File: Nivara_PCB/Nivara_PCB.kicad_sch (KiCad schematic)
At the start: 16 parts, among them J1 NPN_IN, J10 ANALOG_OUT, J11 RELAY, J2 PNP_IN, J3 D_IN, J4 ANALOG_IN, J5 RUN/STOP, J6 FUENTE, J7 NPN_OUT, J8 PNP_OUT, J9 RS485, U4 2920L185DR

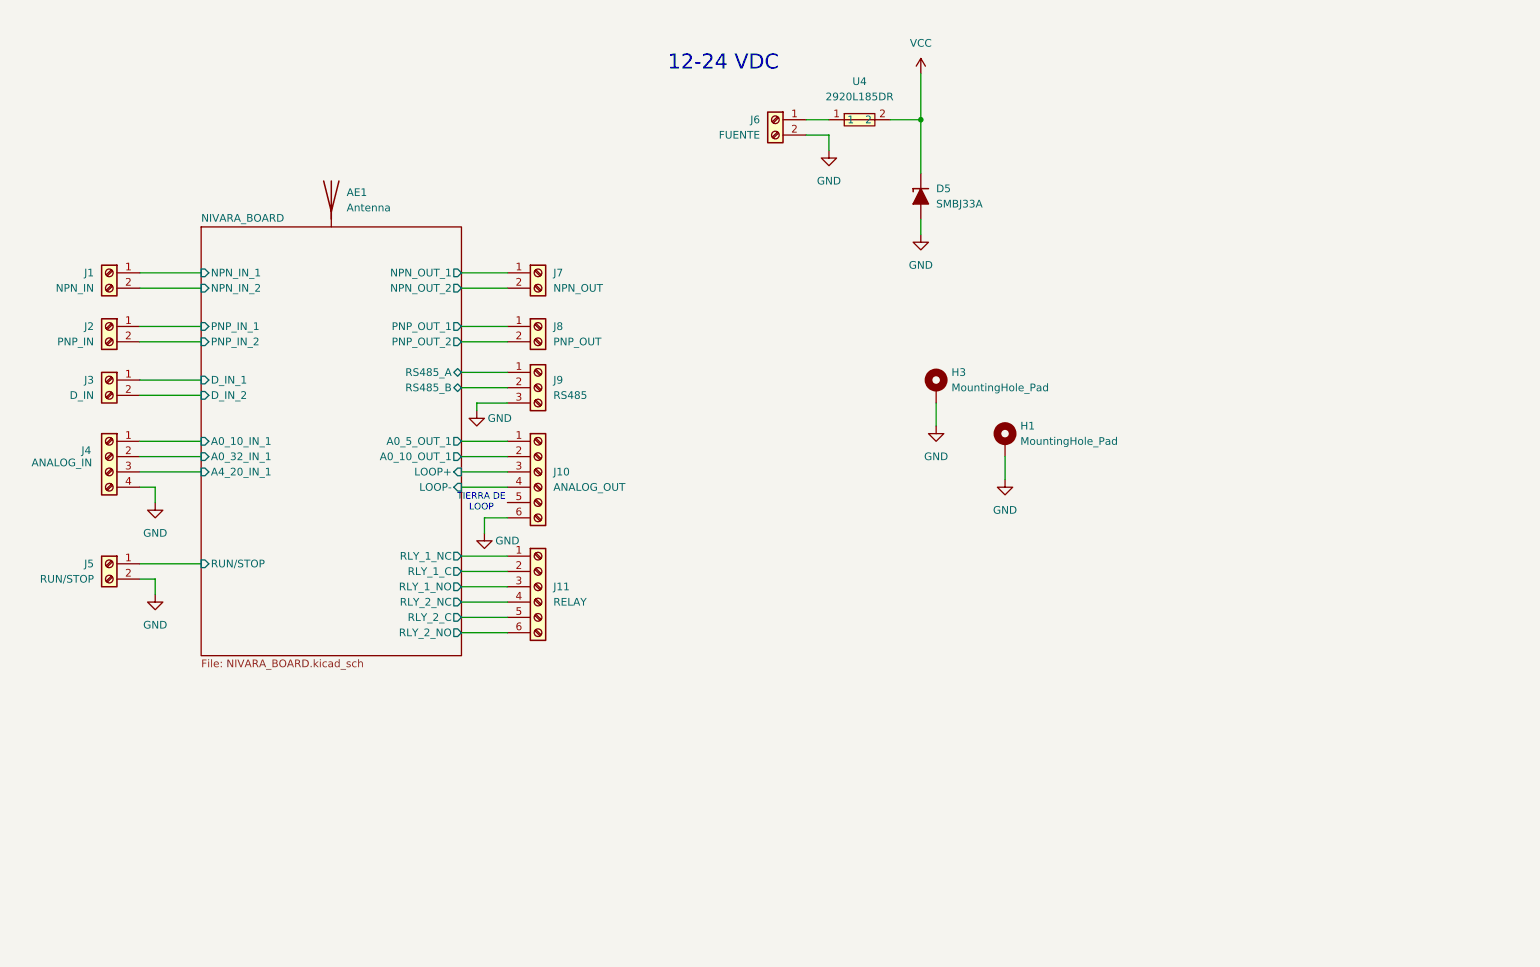
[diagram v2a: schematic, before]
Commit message: Cambios en la medición de voltaje y corriente de la PCB Nivara.
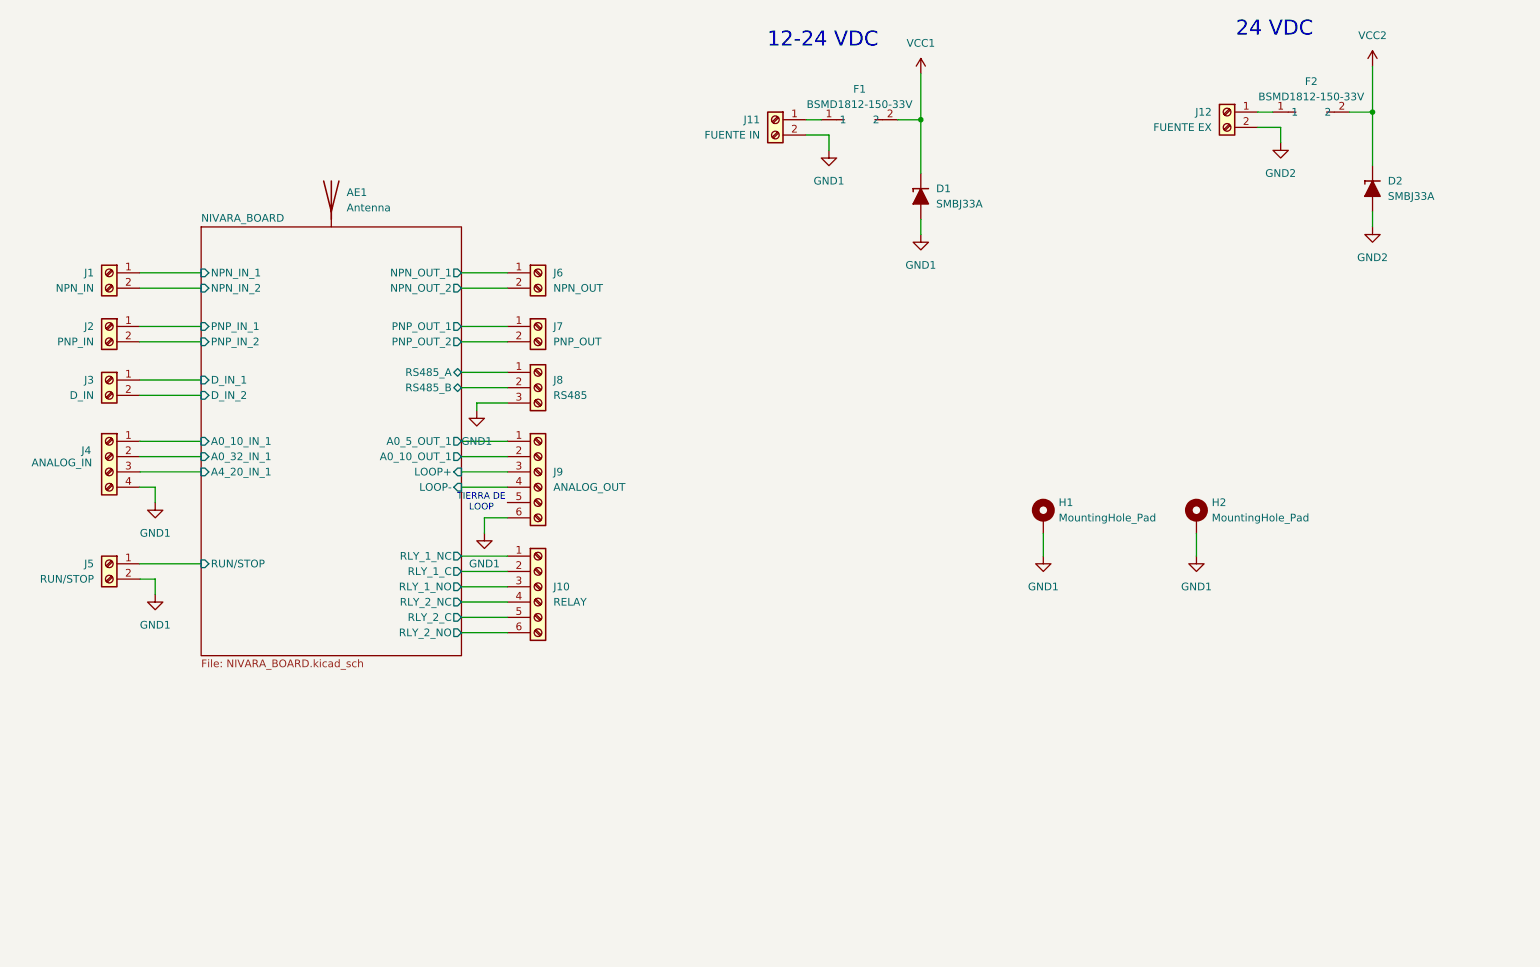
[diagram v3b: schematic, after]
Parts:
- removed U4: 2920L185DR, Fuse_Holder:F2920, symbol Fuse_Holder:2920L185DR
- added D2: SMBJ33A, PCM_Diode_SMD_AKL:D_SMB, symbol PCM_Diode_TVS_AKL:SMBJ33A
- added F1, F2: BSMD1812-150-33V, EasyEDA:F1812, symbol EasyEDA:BSMD1812-150-33V
- added J12: FUENTE EX, TerminalBlock:TerminalBlock_bornier-2_P5.08mm, symbol Connector:Screw_Terminal_01x02
- J11: renamed from J6; value FUENTE -> FUENTE IN
- renumbered D5 to D1, H3 to H1, H1 to H2, J11 to J10, J7 to J6, J8 to J7, J9 to J8, J10 to J9
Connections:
- net at J11.1 (Pin_1): now also F1.1
- net GND renamed GND1
- net VCC renamed VCC1
- net VCC1: now also F1.2
- new net: F2.1, J12.1 (Pin_1)
- new net GND2: D2.2 (A), J12.2 (Pin_2)
- new net VCC2: D2.1 (K), F2.2
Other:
- note added: "24 VDC"
- moved on the sheet: H1, H2

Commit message: New changes to the Nivara PCB schematic files.
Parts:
- removed J9: ANALOG_OUT, TerminalBlock:TerminalBlock_bornier-6_P5.08mm, symbol Connector:Screw_Terminal_01x06
- added C19: 100nF, PCM_Capacitor_SMD_AKL:C_0603_1608Metric, symbol PCM_Capacitor_US_AKL:C_0603
- added D23: SM712, PCM_Package_TO_SOT_SMD_AKL:SOT-23, symbol PCM_Diode_TVS_AKL:SM712
- added J13: USB_C_Receptacle_USB2.0_14P, symbol Connector:USB_C_Receptacle_USB2.0_14P
- added J14: PINHD_1x2_Female, Connector_PinSocket_2.54mm:PinSocket_1x02_P2.54mm_Vertical, symbol PCM_SL_Pin_Headers:PINHD_1x2_Female
- added J9: ANALOG_OUT., TerminalBlock:TerminalBlock_bornier-3_P5.08mm, symbol Connector:Screw_Terminal_01x03
- added R50, R51: 5.1k, PCM_Resistor_SMD_AKL:R_0805_2012Metric, symbol PCM_Resistor_US_AKL:R_0805
- added R52: 10k, PCM_Resistor_SMD_AKL:R_0603_1608Metric, symbol PCM_Resistor_US_AKL:R_0603
- added R53: 14k, PCM_Resistor_SMD_AKL:R_0603_1608Metric, symbol PCM_Resistor_US_AKL:R_0603
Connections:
- net GND1: now also C19.2, D23.3 (Com), J13.A1 (GND), J13.A12 (GND), J13.B1 (GND), J13.B12 (GND), J9.3 (Pin_3), R50.2, R51.2, R53.1
- net NIVARA_BOARD/A0_10_IN_1: now also J4.2 (Pin_2); no longer J4.1 (Pin_1)
- net NIVARA_BOARD/A0_32_IN_1: now also J4.3 (Pin_3); no longer J4.2 (Pin_2)
- net NIVARA_BOARD/A4_20_IN_1: now also J4.1 (Pin_1); no longer J4.3 (Pin_3)
- new net: J13.A4 (VBUS), J13.A9 (VBUS), J13.B4 (VBUS), J13.B9 (VBUS), R52.2
- new net: J13.A5 (CC1), R51.1
- new net: J13.B5 (CC2), R50.1
- new net: C19.1, J13.S1 (SHIELD)
- new net NIVARA_BOARD/A0_V_OUT_1: J9.1 (Pin_1)
- new net NIVARA_BOARD/AUX_1: J14.1
- new net NIVARA_BOARD/AUX_2: J14.2
- new net NIVARA_BOARD/I_OUT: J9.2 (Pin_2)
- new net NIVARA_BOARD/USB_D+: D23.2 (A2), J13.A6 (D+), J13.B6 (D+)
- new net NIVARA_BOARD/USB_D-: D23.1 (A1), J13.A7 (D-), J13.B7 (D-)
- new net NIVARA_BOARD/Vbus: R52.1, R53.2
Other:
- sheet NIVARA_BOARD ports: added A0_V_OUT_1, AUX_1, AUX_2, I_OUT, USB_D+, USB_D-, Vbus; removed A0_10_OUT_1, A0_5_OUT_1, LOOP+, LOOP-
- note removed: "TIERRA DE LOOP"
- moved on the sheet: AE1, H1, H2, J10

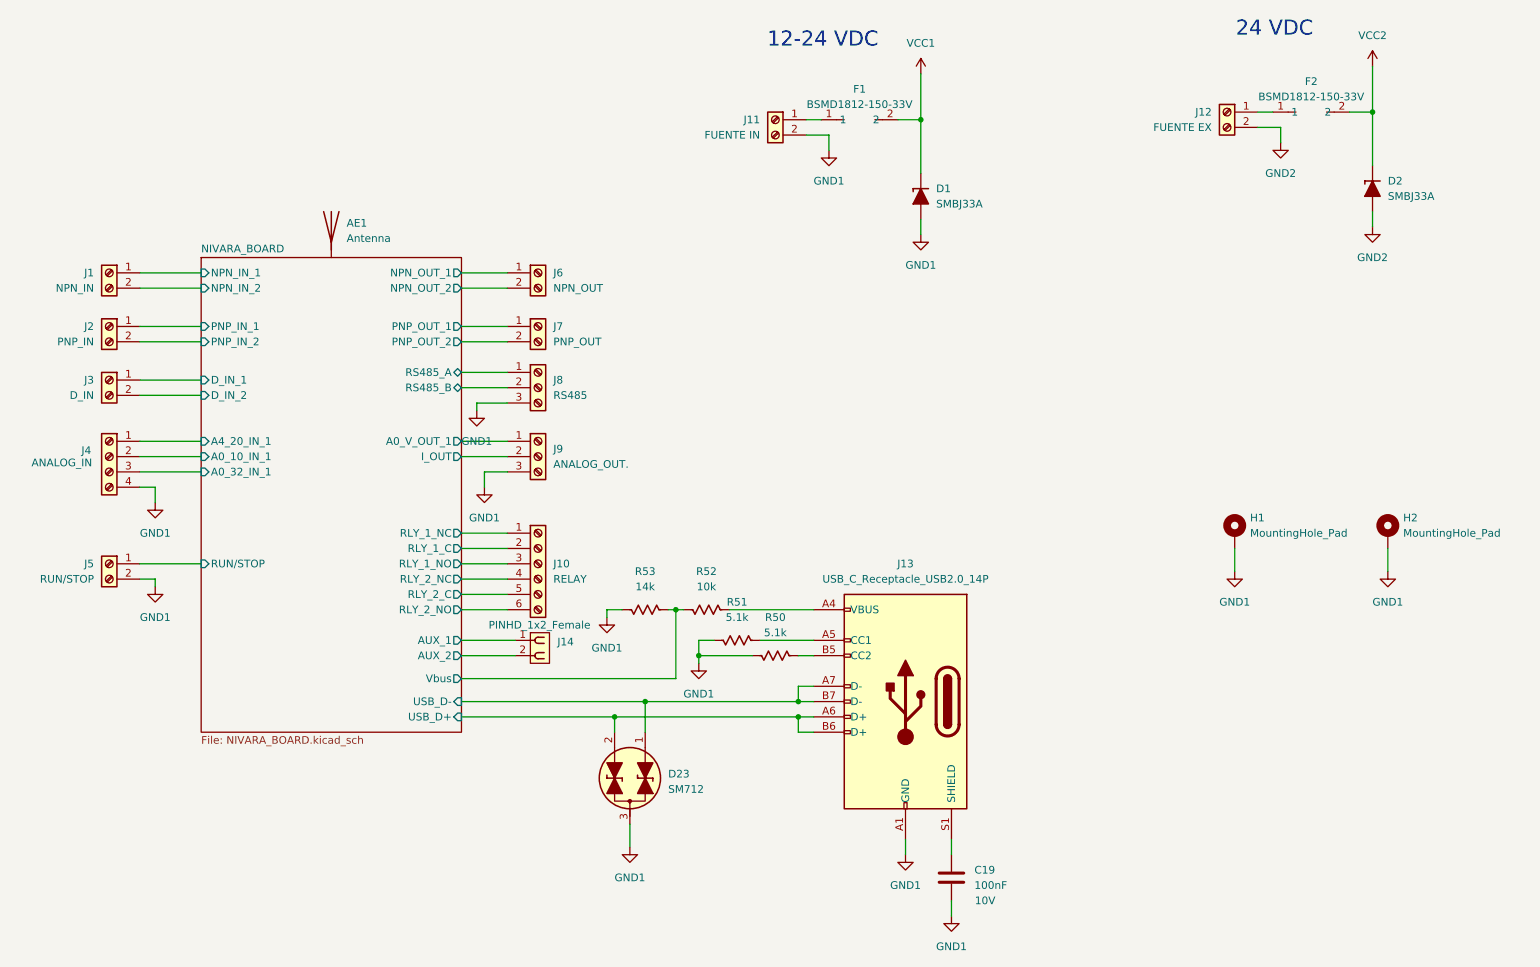
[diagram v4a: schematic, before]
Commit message: Cambios en el PCB de Nivara. Ruteo de emtradas y salidas NPN y PNP.
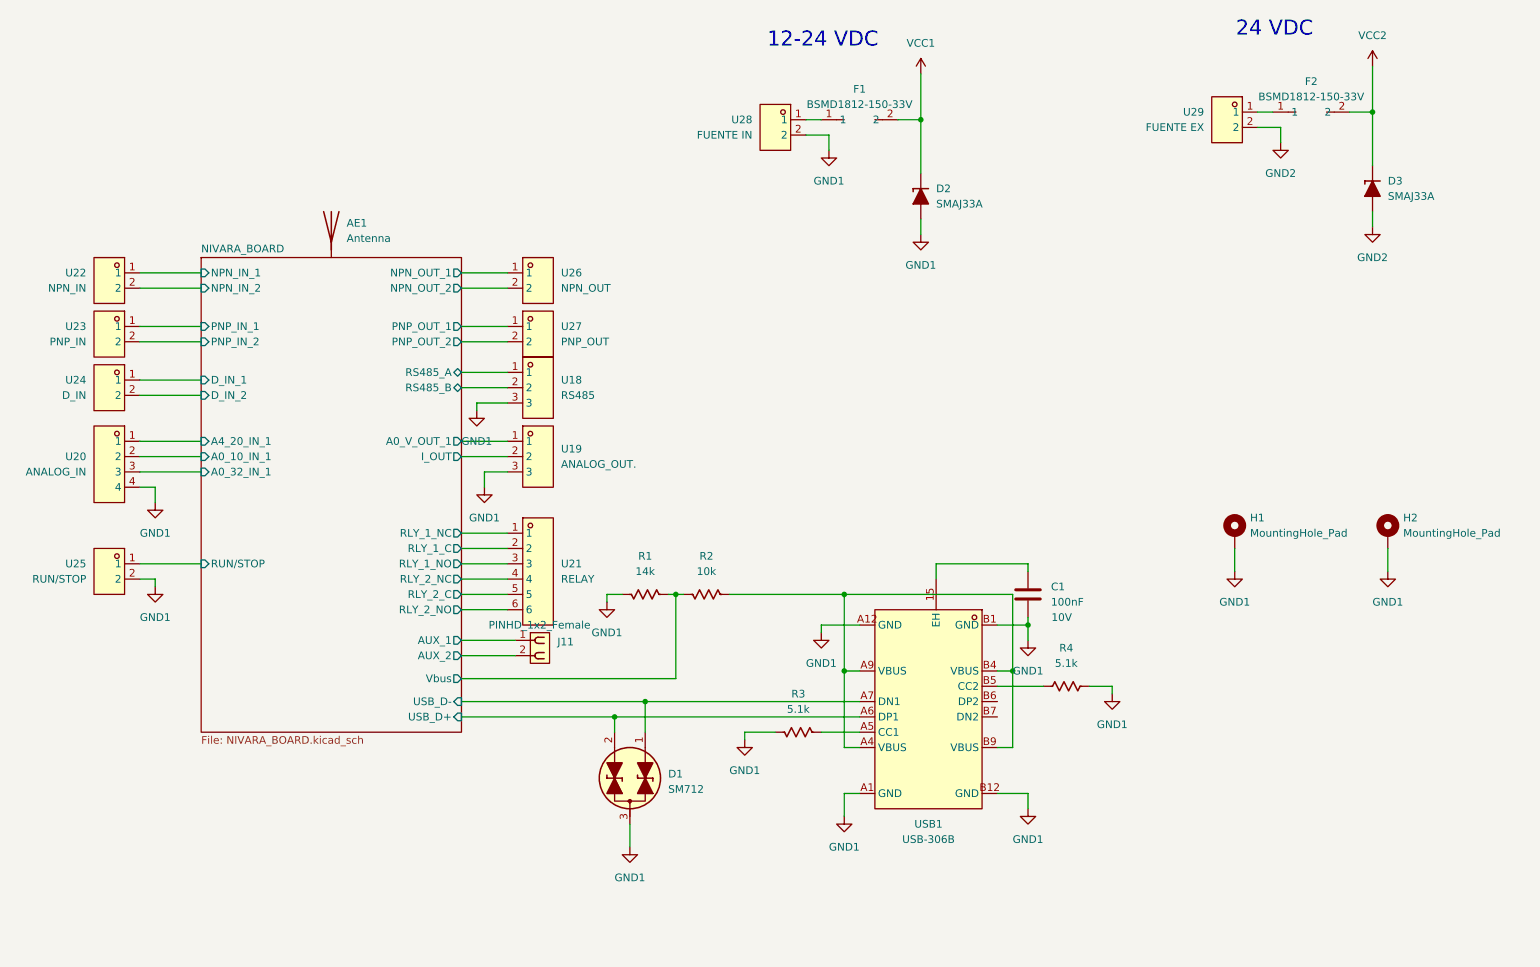
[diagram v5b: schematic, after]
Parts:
- removed D1, D2: SMBJ33A, PCM_Diode_SMD_AKL:D_SMB, symbol PCM_Diode_TVS_AKL:SMBJ33A
- removed J1: NPN_IN, TerminalBlock:TerminalBlock_bornier-2_P5.08mm, symbol Connector:Screw_Terminal_01x02
- removed J10: RELAY, TerminalBlock:TerminalBlock_bornier-6_P5.08mm, symbol Connector:Screw_Terminal_01x06
- removed J11: FUENTE IN, TerminalBlock:TerminalBlock_bornier-2_P5.08mm, symbol Connector:Screw_Terminal_01x02
- removed J12: FUENTE EX, TerminalBlock:TerminalBlock_bornier-2_P5.08mm, symbol Connector:Screw_Terminal_01x02
- removed J13: USB_C_Receptacle_USB2.0_14P, symbol Connector:USB_C_Receptacle_USB2.0_14P
- removed J2: PNP_IN, TerminalBlock:TerminalBlock_bornier-2_P5.08mm, symbol Connector:Screw_Terminal_01x02
- removed J3: D_IN, TerminalBlock:TerminalBlock_bornier-2_P5.08mm, symbol Connector:Screw_Terminal_01x02
- removed J4: ANALOG_IN, TerminalBlock:TerminalBlock_bornier-4_P5.08mm, symbol Connector:Screw_Terminal_01x04
- removed J5: RUN/STOP, TerminalBlock:TerminalBlock_bornier-2_P5.08mm, symbol Connector:Screw_Terminal_01x02
- removed J6: NPN_OUT, TerminalBlock:TerminalBlock_bornier-2_P5.08mm, symbol Connector:Screw_Terminal_01x02
- removed J7: PNP_OUT, TerminalBlock:TerminalBlock_bornier-2_P5.08mm, symbol Connector:Screw_Terminal_01x02
- removed J8: RS485, TerminalBlock:TerminalBlock_bornier-3_P5.08mm, symbol Connector:Screw_Terminal_01x03
- removed J9: ANALOG_OUT., TerminalBlock:TerminalBlock_bornier-3_P5.08mm, symbol Connector:Screw_Terminal_01x03
- added D2, D3: SMAJ33A, PCM_Diode_SMD_AKL:D_SMA, symbol PCM_Diode_TVS_AKL:SMAJ33A
- added U18: RS485, EasyEDA:CONN-TH_XY126V-5.0-3P, symbol EasyEDA:XY126V-5.0-3P
- added U19: ANALOG_OUT., EasyEDA:CONN-TH_XY126V-5.0-3P, symbol EasyEDA:XY126V-5.0-3P
- added U20: ANALOG_IN, EasyEDA:CONN-TH_4P-P5.00_DIBO_DB126V-5.0-4P-GN-P, symbol EasyEDA:DB126V-5.0-4P-GN-P
- added U21: RELAY, EasyEDA:CONN-TH_DB126V-5.0-6P-GN, symbol EasyEDA:DB126V-5.0-6P-GN
- added U22: NPN_IN, EasyEDA:CONN-TH_XY126V-5.0-2P, symbol EasyEDA:XY126V-5.0-2P
- added U23: PNP_IN, EasyEDA:CONN-TH_XY126V-5.0-2P, symbol EasyEDA:XY126V-5.0-2P
- added U24: D_IN, EasyEDA:CONN-TH_XY126V-5.0-2P, symbol EasyEDA:XY126V-5.0-2P
- added U25: RUN/STOP, EasyEDA:CONN-TH_XY126V-5.0-2P, symbol EasyEDA:XY126V-5.0-2P
- added U26: NPN_OUT, EasyEDA:CONN-TH_XY126V-5.0-2P, symbol EasyEDA:XY126V-5.0-2P
- added U27: PNP_OUT, EasyEDA:CONN-TH_XY126V-5.0-2P, symbol EasyEDA:XY126V-5.0-2P
- added U28: FUENTE IN, EasyEDA:CONN-TH_XY126V-5.0-2P, symbol EasyEDA:XY126V-5.0-2P
- added U29: FUENTE EX, EasyEDA:CONN-TH_XY126V-5.0-2P, symbol EasyEDA:XY126V-5.0-2P
- added USB1: USB-306B, EasyEDA:USB-TYPE-C-TH_USB-306B, symbol EasyEDA:USB-306B
- renumbered C19 to C1, D23 to D1, J14 to J11, R53 to R1, R52 to R2, R50 to R3, R51 to R4
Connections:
- net GND1: now also D2.2 (A), U18.3, U19.3, U20.4, U25.2, U28.2, USB1.A1 (GND), USB1.A12 (GND), USB1.B1 (GND), USB1.B12 (GND)
- net GND2: now also D3.2 (A), U29.2
- net NIVARA_BOARD/A0_10_IN_1: now also U20.2
- net NIVARA_BOARD/A0_32_IN_1: now also U20.3
- net NIVARA_BOARD/A0_V_OUT_1: now also U19.1
- net NIVARA_BOARD/A4_20_IN_1: now also U20.1
- net NIVARA_BOARD/D_IN_1: now also U24.1
- net NIVARA_BOARD/D_IN_2: now also U24.2
- net NIVARA_BOARD/I_OUT: now also U19.2
- net NIVARA_BOARD/NPN_IN_1: now also U22.1
- net NIVARA_BOARD/NPN_IN_2: now also U22.2
- net NIVARA_BOARD/NPN_OUT_1: now also U26.1
- net NIVARA_BOARD/NPN_OUT_2: now also U26.2
- net NIVARA_BOARD/PNP_IN_1: now also U23.1
- net NIVARA_BOARD/PNP_IN_2: now also U23.2
- net NIVARA_BOARD/PNP_OUT_1: now also U27.1
- net NIVARA_BOARD/PNP_OUT_2: now also U27.2
- net NIVARA_BOARD/RLY_1_C: now also U21.2
- net NIVARA_BOARD/RLY_1_NC: now also U21.1
- net NIVARA_BOARD/RLY_1_NO: now also U21.3
- net NIVARA_BOARD/RLY_2_C: now also U21.5
- net NIVARA_BOARD/RLY_2_NC: now also U21.4
- net NIVARA_BOARD/RLY_2_NO: now also U21.6
- net NIVARA_BOARD/RS485_A: now also U18.1
- net NIVARA_BOARD/RS485_B: now also U18.2
- net NIVARA_BOARD/RUN/STOP: now also U25.1
- net NIVARA_BOARD/USB_D+: now also USB1.A6 (DP1)
- net NIVARA_BOARD/USB_D-: now also USB1.A7 (DN1)
- net VCC1: now also D2.1 (K)
- net VCC2: now also D3.1 (K)
- net at R2.2: now also USB1.A4 (VBUS), USB1.A9 (VBUS), USB1.B4 (VBUS), USB1.B9 (VBUS)
- net at R4.1: now also USB1.B5 (CC2)
- net at R3.1: now also USB1.A5 (CC1)
- net at C1.1: now also USB1.15 (EH)
- net at F1.1: now also U28.1
- net at F2.1: now also U29.1
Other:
- moved on the sheet: C1, R1, R2, R3, R4

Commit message: Modificación del PCB.
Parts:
- removed USB1: USB-306B, EasyEDA:USB-TYPE-C-TH_USB-306B, symbol EasyEDA:USB-306B
- added U30: GT-USB-7010ASV, EasyEDA:USB-C-SMD_G-SWITCH_GT-USB-7010ASV, symbol EasyEDA:GT-USB-7010ASV
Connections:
- net GND1: now also U30.A1B12 (GND), U30.B1A12 (GND)
- net NIVARA_BOARD/USB_D+: now also D1.1 (A1), U30.A6 (DP1); no longer D1.2 (A2)
- net NIVARA_BOARD/USB_D-: now also D1.2 (A2), U30.A7 (DN1); no longer D1.1 (A1)
- net at C1.1: now also U30.1 (SHELL), U30.2 (SHELL), U30.3 (SHELL), U30.4 (SHELL)
- net at R2.2: now also U30.A4B9 (VBUS), U30.B4A9 (VBUS)
- net at R3.1: now also U30.B5 (CC2)
- net at R4.1: now also U30.A5 (CC1)
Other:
- moved on the sheet: C1, R3, R4
